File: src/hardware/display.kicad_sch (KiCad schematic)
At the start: 6 parts, among them J1 046809612110846+, U6 TXS0108ERKSR, U7 LP5817YCHR

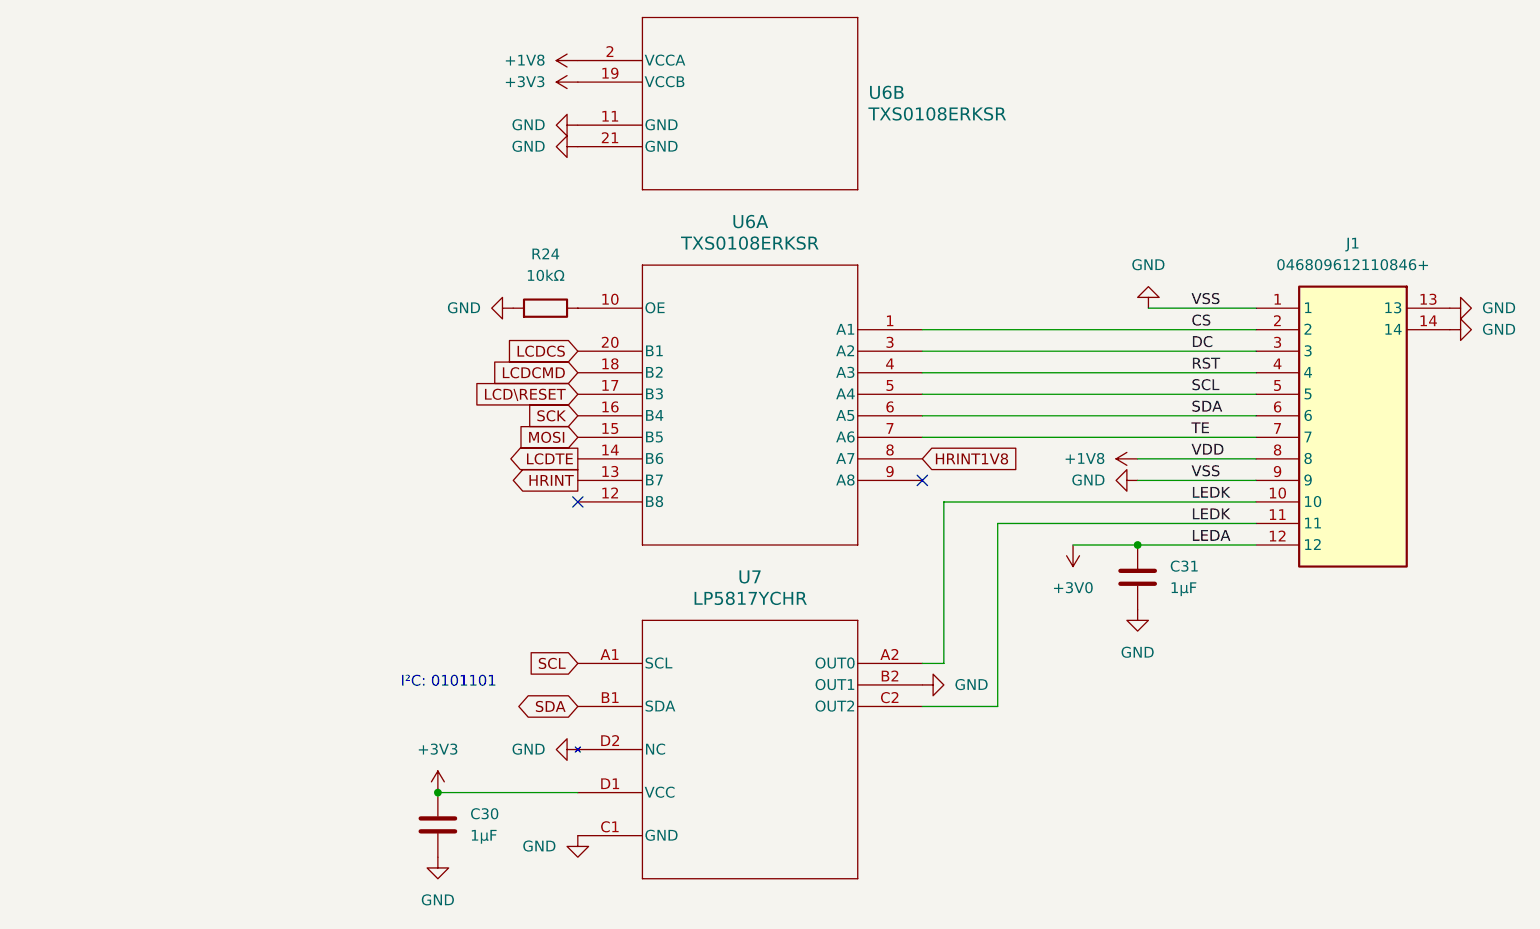
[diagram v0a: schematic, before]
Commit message: Cleanup & Fixes; Changed GPIO; Added Camera; Added Microphone
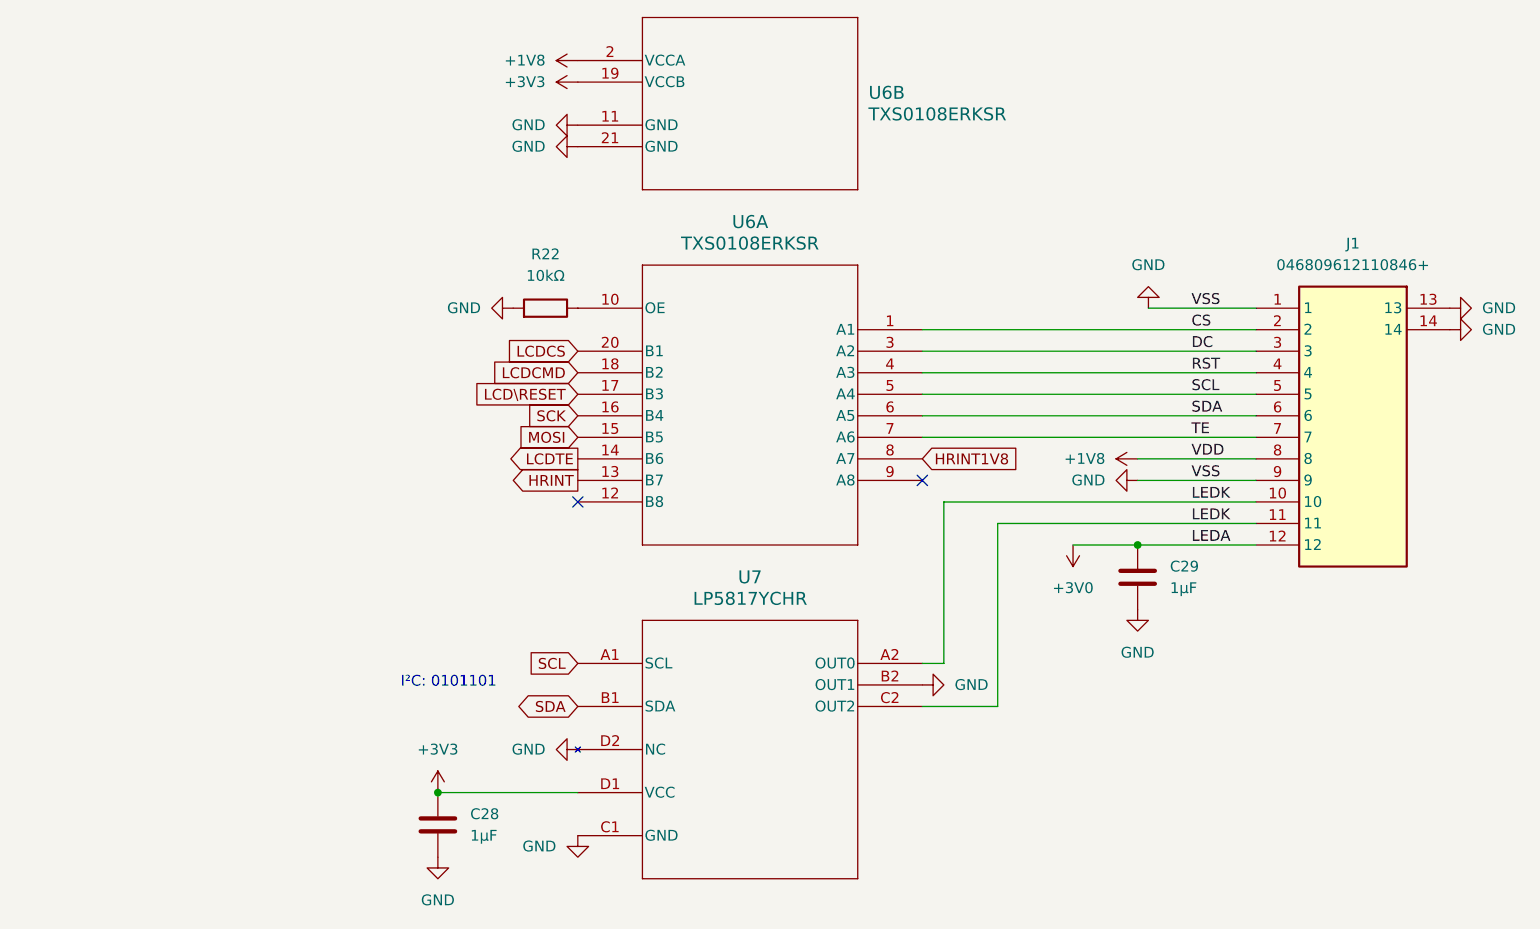
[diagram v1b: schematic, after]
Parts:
- renumbered C30 to C28, C31 to C29, R24 to R22
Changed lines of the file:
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@@
 		(dnp no)
 		(fields_autoplaced yes)
-		(property "Reference" "#PWR083"
+		(property "Reference" "#PWR079"
 			(at 90.17 130.81 0)
 			(effects
@@
 			(project "raywatch"
 				(path "/7b654ee8-2a53-4d39-8b7d-32c7bb3cb0ed/0522506d-d6b7-4115-aecc-a1b886294452"
-					(reference "#PWR083")
+					(reference "#PWR079")
 					(unit 1)
 				)
@@
 		(dnp no)
 		(fields_autoplaced yes)
-		(property "Reference" "#PWR098"
+		(property "Reference" "#PWR094"
 			(at 215.9 69.85 0)
 			(effects
@@
 			(project "raywatch"
 				(path "/7b654ee8-2a53-4d39-8b7d-32c7bb3cb0ed/0522506d-d6b7-4115-aecc-a1b886294452"
-					(reference "#PWR098")
+					(reference "#PWR094")
 					(unit 1)
 				)
@@
 		(dnp no)
 		(fields_autoplaced yes)
-		(property "Reference" "#PWR086"
+		(property "Reference" "#PWR082"
 			(at 110.49 40.64 0)
 			(effects
@@
 			(project "raywatch"
 				(path "/7b654ee8-2a53-4d39-8b7d-32c7bb3cb0ed/0522506d-d6b7-4115-aecc-a1b886294452"
-					(reference "#PWR086")
+					(reference "#PWR082")
 					(unit 1)
 				)
@@
 		(dnp no)
 		(fields_autoplaced yes)
-		(property "Reference" "R24"
+		(property "Reference" "R22"
 			(at 102.87 63.5 90)
 			(effects
@@
 			(project "raywatch"
 				(path "/7b654ee8-2a53-4d39-8b7d-32c7bb3cb0ed/0522506d-d6b7-4115-aecc-a1b886294452"
-					(reference "R24")
+					(reference "R22")
 					(unit 1)
 				)
@@
 		(dnp no)
 		(fields_autoplaced yes)
-		(property "Reference" "#PWR084"
+		(property "Reference" "#PWR080"
 			(at 90.17 140.97 0)
 			(effects
@@
 			(project "raywatch"
 				(path "/7b654ee8-2a53-4d39-8b7d-32c7bb3cb0ed/0522506d-d6b7-4115-aecc-a1b886294452"
-					(reference "#PWR084")
+					(reference "#PWR080")
 					(unit 1)
 				)
@@
 		(dnp no)
 		(fields_autoplaced yes)
-		(property "Reference" "#PWR091"
+		(property "Reference" "#PWR087"
 			(at 106.68 138.43 0)
 			(effects
@@
 			(project "raywatch"
 				(path "/7b654ee8-2a53-4d39-8b7d-32c7bb3cb0ed/0522506d-d6b7-4115-aecc-a1b886294452"
-					(reference "#PWR091")
+					(reference "#PWR087")
 					(unit 1)
 				)
@@
 		(dnp no)
 		(fields_autoplaced yes)
-		(property "Reference" "#PWR094"
+		(property "Reference" "#PWR090"
 			(at 176.53 87.63 0)
 			(effects
@@
 			(project "raywatch"
 				(path "/7b654ee8-2a53-4d39-8b7d-32c7bb3cb0ed/0522506d-d6b7-4115-aecc-a1b886294452"
-					(reference "#PWR094")
+					(reference "#PWR090")
 					(unit 1)
 				)
@@
 		(dnp no)
 		(fields_autoplaced yes)
-		(property "Reference" "#PWR093"
+		(property "Reference" "#PWR088"
 			(at 153.67 114.3 0)
 			(effects
@@
 			(project "raywatch"
 				(path "/7b654ee8-2a53-4d39-8b7d-32c7bb3cb0ed/0522506d-d6b7-4115-aecc-a1b886294452"
-					(reference "#PWR093")
+					(reference "#PWR088")
 					(unit 1)
 				)
@@
 		(dnp no)
 		(fields_autoplaced yes)
-		(property "Reference" "#PWR087"
+		(property "Reference" "#PWR083"
 			(at 110.49 43.18 0)
 			(effects
@@
 			(project "raywatch"
 				(path "/7b654ee8-2a53-4d39-8b7d-32c7bb3cb0ed/0522506d-d6b7-4115-aecc-a1b886294452"
-					(reference "#PWR087")
+					(reference "#PWR083")
 					(unit 1)
 				)
@@
 		(dnp no)
 		(fields_autoplaced yes)
-		(property "Reference" "#PWR088"
+		(property "Reference" "#PWR084"
 			(at 100.33 48.26 0)
 			(effects
@@
 			(project "raywatch"
 				(path "/7b654ee8-2a53-4d39-8b7d-32c7bb3cb0ed/0522506d-d6b7-4115-aecc-a1b886294452"
-					(reference "#PWR088")
+					(reference "#PWR084")
 					(unit 1)
 				)
@@
 		(dnp no)
 		(fields_autoplaced yes)
-		(property "Reference" "#PWR092"
+		(property "Reference" "#PWR089"
 			(at 165.1 93.98 0)
 			(effects
@@
 			(project "raywatch"
 				(path "/7b654ee8-2a53-4d39-8b7d-32c7bb3cb0ed/0522506d-d6b7-4115-aecc-a1b886294452"
-					(reference "#PWR092")
+					(reference "#PWR089")
 					(unit 1)
 				)
@@
 		(dnp no)
 		(fields_autoplaced yes)
-		(property "Reference" "C31"
+		(property "Reference" "C29"
 			(at 176.53 100.3299 0)
 			(effects
@@
 			(project "raywatch"
 				(path "/7b654ee8-2a53-4d39-8b7d-32c7bb3cb0ed/0522506d-d6b7-4115-aecc-a1b886294452"
-					(reference "C31")
+					(reference "C29")
 					(unit 1)
 				)
@@
 		(dnp no)
 		(fields_autoplaced yes)
-		(property "Reference" "#PWR085"
+		(property "Reference" "#PWR081"
 			(at 92.71 69.85 0)
 			(effects
@@
 			(project "raywatch"
 				(path "/7b654ee8-2a53-4d39-8b7d-32c7bb3cb0ed/0522506d-d6b7-4115-aecc-a1b886294452"
-					(reference "#PWR085")
+					(reference "#PWR081")
 					(unit 1)
 				)
@@
 		(dnp no)
 		(fields_autoplaced yes)
-		(property "Reference" "#PWR089"
+		(property "Reference" "#PWR085"
 			(at 100.33 50.8 0)
 			(effects
@@
 			(project "raywatch"
 				(path "/7b654ee8-2a53-4d39-8b7d-32c7bb3cb0ed/0522506d-d6b7-4115-aecc-a1b886294452"
-					(reference "#PWR089")
+					(reference "#PWR085")
 					(unit 1)
 				)
@@
 		(dnp no)
 		(fields_autoplaced yes)
-		(property "Reference" "#PWR095"
+		(property "Reference" "#PWR091"
 			(at 166.37 90.17 0)
 			(effects
@@
 			(project "raywatch"
 				(path "/7b654ee8-2a53-4d39-8b7d-32c7bb3cb0ed/0522506d-d6b7-4115-aecc-a1b886294452"
-					(reference "#PWR095")
+					(reference "#PWR091")
 					(unit 1)
 				)
@@
 		(dnp no)
 		(fields_autoplaced yes)
-		(property "Reference" "C30"
+		(property "Reference" "C28"
 			(at 93.98 129.5399 0)
 			(effects
@@
 			(project "raywatch"
 				(path "/7b654ee8-2a53-4d39-8b7d-32c7bb3cb0ed/0522506d-d6b7-4115-aecc-a1b886294452"
-					(reference "C30")
+					(reference "C28")
 					(unit 1)
 				)
@@
 		(dnp no)
 		(fields_autoplaced yes)
-		(property "Reference" "#PWR099"
+		(property "Reference" "#PWR095"
 			(at 215.9 72.39 0)
 			(effects
@@
 			(project "raywatch"
 				(path "/7b654ee8-2a53-4d39-8b7d-32c7bb3cb0ed/0522506d-d6b7-4115-aecc-a1b886294452"
-					(reference "#PWR099")
+					(reference "#PWR095")
 					(unit 1)
 				)
@@
 		(dnp no)
 		(fields_autoplaced yes)
-		(property "Reference" "#PWR090"
+		(property "Reference" "#PWR086"
 			(at 100.33 121.92 0)
 			(effects
@@
 			(project "raywatch"
 				(path "/7b654ee8-2a53-4d39-8b7d-32c7bb3cb0ed/0522506d-d6b7-4115-aecc-a1b886294452"
-					(reference "#PWR090")
+					(reference "#PWR086")
 					(unit 1)
 				)
@@
 		(dnp no)
 		(fields_autoplaced yes)
-		(property "Reference" "#PWR097"
+		(property "Reference" "#PWR093"
 			(at 173.99 63.5 0)
 			(effects
@@
 			(project "raywatch"
 				(path "/7b654ee8-2a53-4d39-8b7d-32c7bb3cb0ed/0522506d-d6b7-4115-aecc-a1b886294452"
-					(reference "#PWR097")
+					(reference "#PWR093")
 					(unit 1)
 				)
@@
 		(dnp no)
 		(fields_autoplaced yes)
-		(property "Reference" "#PWR096"
+		(property "Reference" "#PWR092"
 			(at 172.72 111.76 0)
 			(effects
@@
 			(project "raywatch"
 				(path "/7b654ee8-2a53-4d39-8b7d-32c7bb3cb0ed/0522506d-d6b7-4115-aecc-a1b886294452"
-					(reference "#PWR096")
-					(unit 1)
-				)
+					(reference "#PWR092")
+					(unit 1)
+				)

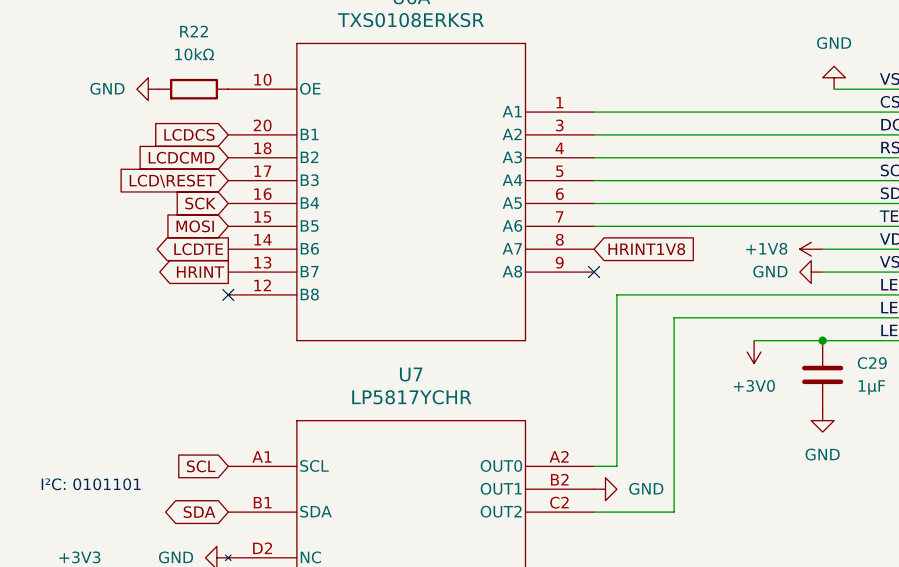
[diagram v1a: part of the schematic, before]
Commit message: Added 1.8V GPIO Extender
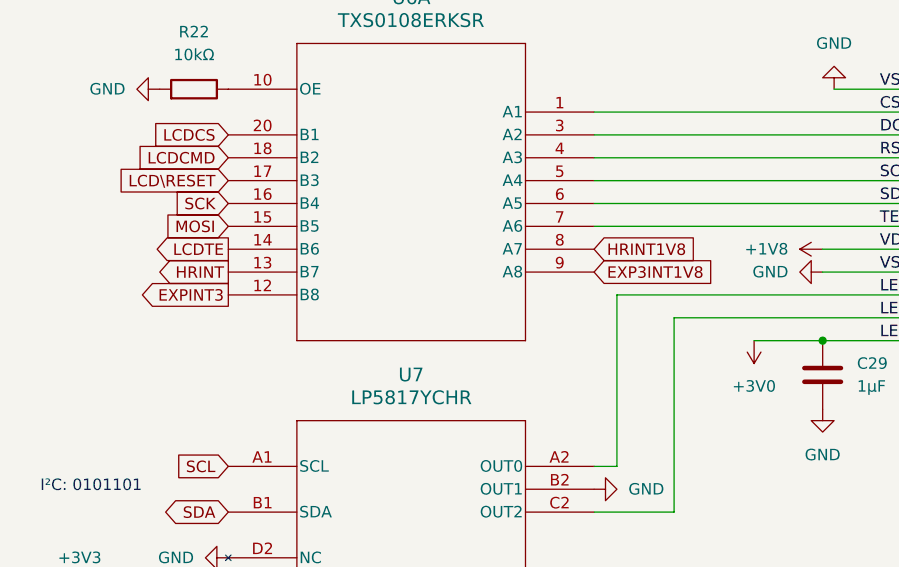
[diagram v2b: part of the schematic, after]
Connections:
- net EXPINT3: now reaches U6.12 (B8)
- net EXP3INT1V8: now reaches U6.9 (A8)
- no-connect marks 2 -> 0
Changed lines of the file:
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@@
 		(color 0 0 0 0)
-	)
-	(no_connect
-		(at 147.32 90.17)
-	)
-	(no_connect
-		(at 106.68 92.71)
 	)
 	(wire
@@
 			(effects
 				(font
+					(size 1.27 1.27)
+				)
+				(justify right)
+				(hide yes)
+			)
+		)
+	)
+	(global_label "EXP3INT1V8"
+		(shape input)
+		(at 147.32 90.17 0)
+		(fields_autoplaced yes)
+		(effects
+			(font
+				(size 1.27 1.27)
+			)
+			(justify left)
+		)
+		(property "Intersheetrefs" "${INTERSHEET_REFS}"
+			(at 161.5537 90.17 0)
+			(effects
+				(font
+					(size 1.27 1.27)
+				)
+				(justify left)
+				(hide yes)
+			)
+		)
+	)
+	(global_label "EXPINT3"
+		(shape output)
+		(at 106.68 92.71 180)
+		(fields_autoplaced yes)
+		(effects
+			(font
+				(size 1.27 1.27)
+			)
+			(justify right)
+		)
+		(property "Intersheetrefs" "${INTERSHEET_REFS}"
+			(at 95.9539 92.71 0)
+			(effects
+				(font

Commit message: Removed Camera because currently not viable
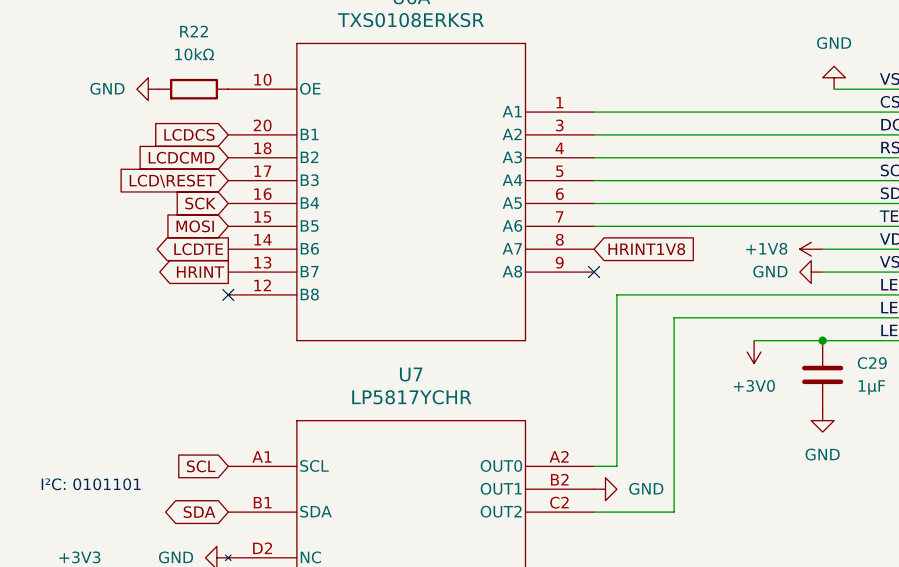
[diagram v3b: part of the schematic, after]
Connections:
- net EXP3INT1V8: no longer names the net of U6.9 (A8)
- net EXPINT3: no longer names the net of U6.12 (B8)
- no-connect marks 0 -> 2
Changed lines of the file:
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@@
 		(color 0 0 0 0)
+	)
+	(no_connect
+		(at 147.32 90.17)
+	)
+	(no_connect
+		(at 106.68 92.71)
 	)
 	(wire
@@
 		)
 	)
+	(global_label "HRINT"
+		(shape output)
+		(at 106.68 90.17 180)
+		(fields_autoplaced yes)
+		(effects
+			(font
+				(size 1.27 1.27)
+			)
+			(justify right)
+		)
+		(property "Intersheetrefs" "${INTERSHEET_REFS}"
+			(at 98.1914 90.17 0)
+			(effects
+				(font
+					(size 1.27 1.27)
+				)
+				(justify right)
+				(hide yes)
+			)
+		)
+	)
 	(global_label "LCD\\RESET"
 		(shape input)
@@
 			(effects
 				(font
-					(size 1.27 1.27)
-				)
-				(justify right)
-				(hide yes)
-			)
-		)
-	)
-	(global_label "HRINT"
-		(shape output)
-		(at 106.68 90.17 180)
-		(fields_autoplaced yes)
-		(effects
-			(font
-				(size 1.27 1.27)
-			)
-			(justify right)
-		)
-		(property "Intersheetrefs" "${INTERSHEET_REFS}"
-			(at 98.1914 90.17 0)
-			(effects
-				(font
-					(size 1.27 1.27)
-				)
-				(justify right)
-				(hide yes)
-			)
-		)
-	)
-	(global_label "EXP3INT1V8"
-		(shape input)
-		(at 147.32 90.17 0)
-		(fields_autoplaced yes)
-		(effects
-			(font
-				(size 1.27 1.27)
-			)
-			(justify left)
-		)
-		(property "Intersheetrefs" "${INTERSHEET_REFS}"
-			(at 161.5537 90.17 0)
-			(effects
-				(font
-					(size 1.27 1.27)
-				)
-				(justify left)
-				(hide yes)
-			)
-		)
-	)
-	(global_label "EXPINT3"
-		(shape output)
-		(at 106.68 92.71 180)
-		(fields_autoplaced yes)
-		(effects
-			(font
-				(size 1.27 1.27)
-			)
-			(justify right)
-		)
-		(property "Intersheetrefs" "${INTERSHEET_REFS}"
-			(at 95.9539 92.71 0)
-			(effects
-				(font
